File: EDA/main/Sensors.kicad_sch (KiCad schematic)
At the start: 13 parts, among them U2 ICM-42688-PC, U3 MMC5983MA, U4 TMP121AIDBVR, U5 TMP121AIDBVR, U6 BMP581

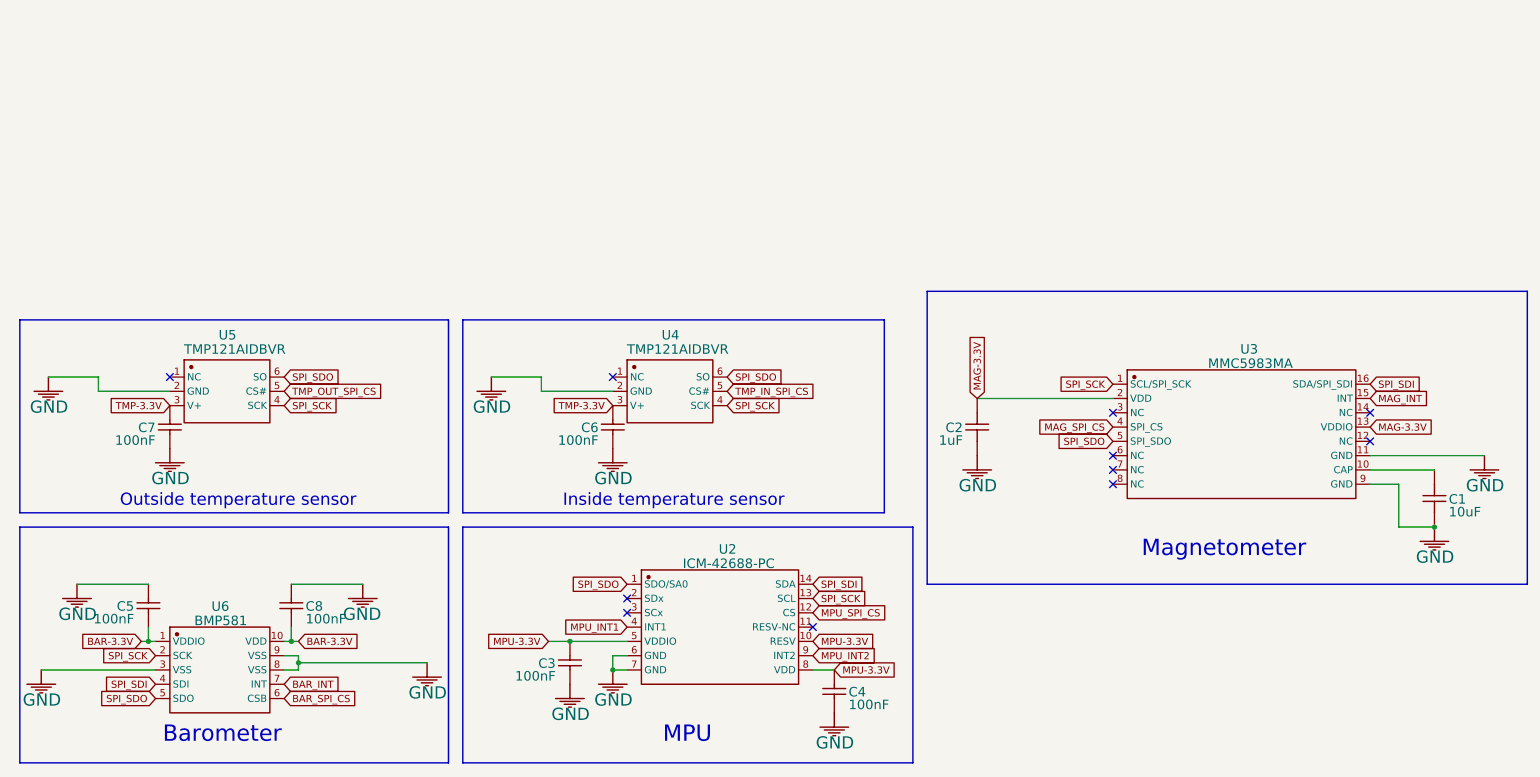
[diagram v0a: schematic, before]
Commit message: Project restructure, and added a bottom assembly PCB.
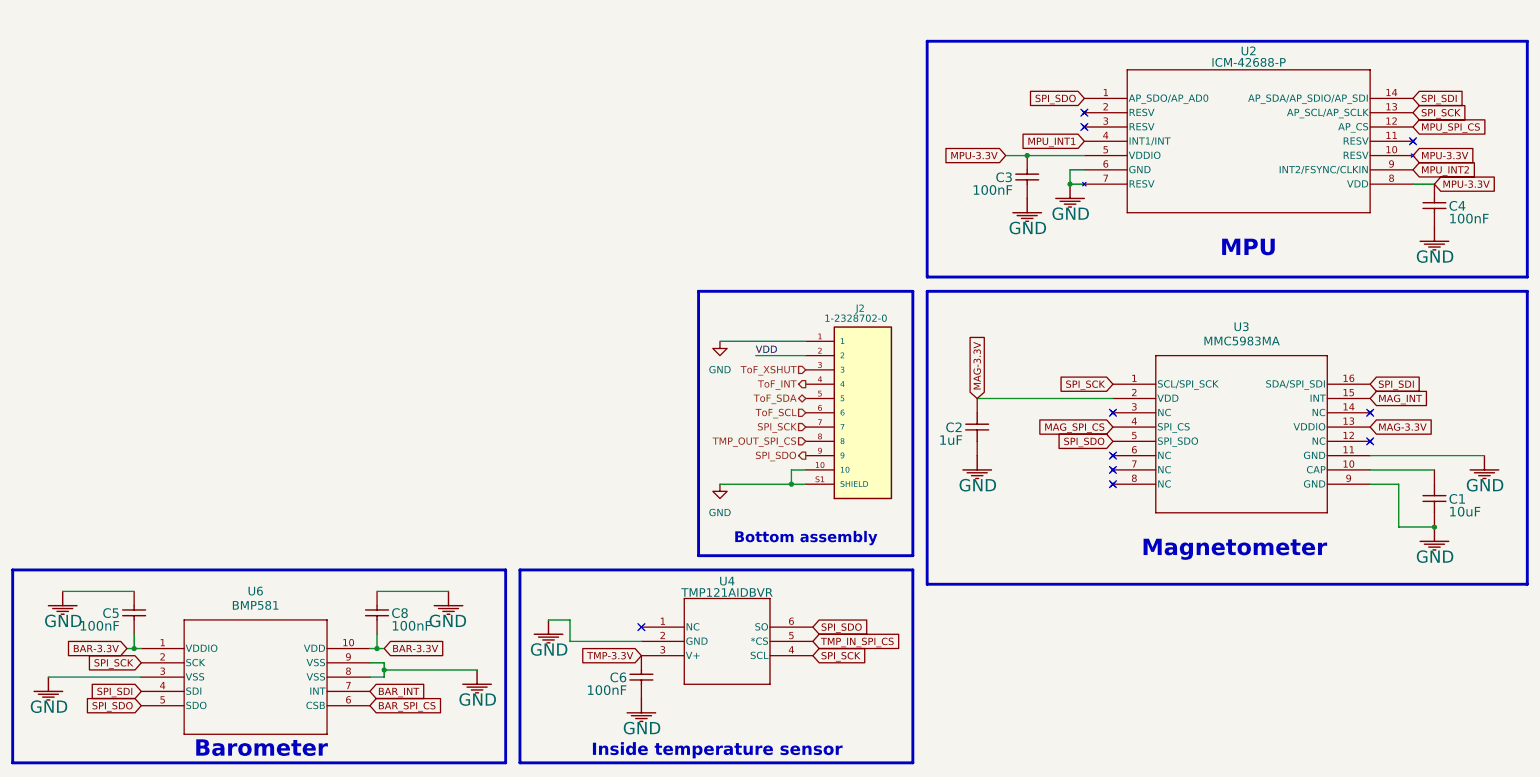
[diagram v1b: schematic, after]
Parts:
- removed C7: 100nF, symbol CL10B104JB8NNNC_4
- removed U2: ICM-42688-PC, symbol ICM-42688-PC
- removed U3: MMC5983MA, symbol MMC5983MA
- removed U4: TMP121AIDBVR, symbol TMP121AIDBVR
- removed U5: TMP121AIDBVR, symbol TMP121AIDBVR_1
- removed U6: BMP581, symbol BMP581
- added J2: 1-2328702-0, CANSAT-lib:TE_1-2328702-0, symbol CANSAT-lib:1-2328702-0
- added U2: ICM-42688-P, CANSAT-lib:LGA14_2P5X3X0P91_TDK, symbol CANSAT-lib:ICM-42688-P
- added U3: MMC5983MA, CANSAT-lib:MMC5983MA_MEM, symbol CANSAT-lib:MMC5983MA
- added U4: TMP121AIDBVR, CANSAT-lib:DBV6, symbol CANSAT-lib:TMP121AIDBVR
- added U6: BMP581, CANSAT-lib:QFN10_BMP581_BOS, symbol CANSAT-lib:BMP581
- C1, C2: footprint (none) -> Capacitor_SMD:C_0603_1608Metric
- C3, C4, C5, C6, C8: footprint (none) -> Capacitor_SMD:C_0402_1005Metric
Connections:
- net BAR-3.3V: now also U6.1 (VDDIO), U6.10 (VDD)
- net BAR_INT: now also U6.7 (INT)
- net BAR_SPI_CS: now also U6.6 (CSB)
- net GND: now also J2.1, J2.10, J2.S1 (SHIELD), J2.S2 (SHIELD), U2.6 (GND), U2.7 (RESV), U3.11 (GND), U3.9 (GND), U4.2 (GND), U6.3 (VSS), U6.8 (VSS), U6.9 (VSS)
- net MAG-3.3V: now also U3.13 (VDDIO), U3.2 (VDD)
- net MAG_INT: now also U3.15 (INT)
- net MAG_SPI_CS: now also U3.4 (SPI_CS)
- net MPU-3.3V: now also U2.10 (RESV), U2.5 (VDDIO), U2.8 (VDD)
- net MPU_INT1: now also U2.4 (INT1/INT)
- net MPU_INT2: now also U2.9 (INT2/FSYNC/CLKIN)
- net MPU_SPI_CS: now also U2.12 (AP_CS)
- net SPI_SCK: now also J2.7, U2.13 (AP_SCL/AP_SCLK), U3.1 (SCL/SPI_SCK), U4.4 (SCL), U6.2 (SCK)
- net SPI_SDI: now also U2.14 (AP_SDA/AP_SDIO/AP_SDI), U3.16 (SDA/SPI_SDI), U6.4 (SDI)
- net SPI_SDO: now also J2.9, U2.1 (AP_SDO/AP_AD0), U3.5 (SPI_SDO), U4.6 (SO), U6.5 (SDO)
- net TMP-3.3V: now also U4.3 (V+)
- net TMP_IN_SPI_CS: now also U4.5 (*CS)
- net TMP_OUT_SPI_CS: now also J2.8
- net at C1.2: now also U3.10 (CAP)
- new net ToF_INT: J2.4
- new net ToF_SCL: J2.6
- new net ToF_SDA: J2.5
- new net ToF_XSHUT: J2.3
- new net VDD: J2.2
- no-connect marks 11 -> 10
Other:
- note added: "Bottom assembly"
- note removed: "Outside temperature sensor"
- moved on the sheet: C3, C4, C5, C6, C8

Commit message: Assigned CS and INT from sensors, and added SWD to PWR-MCU and CORE-MCU
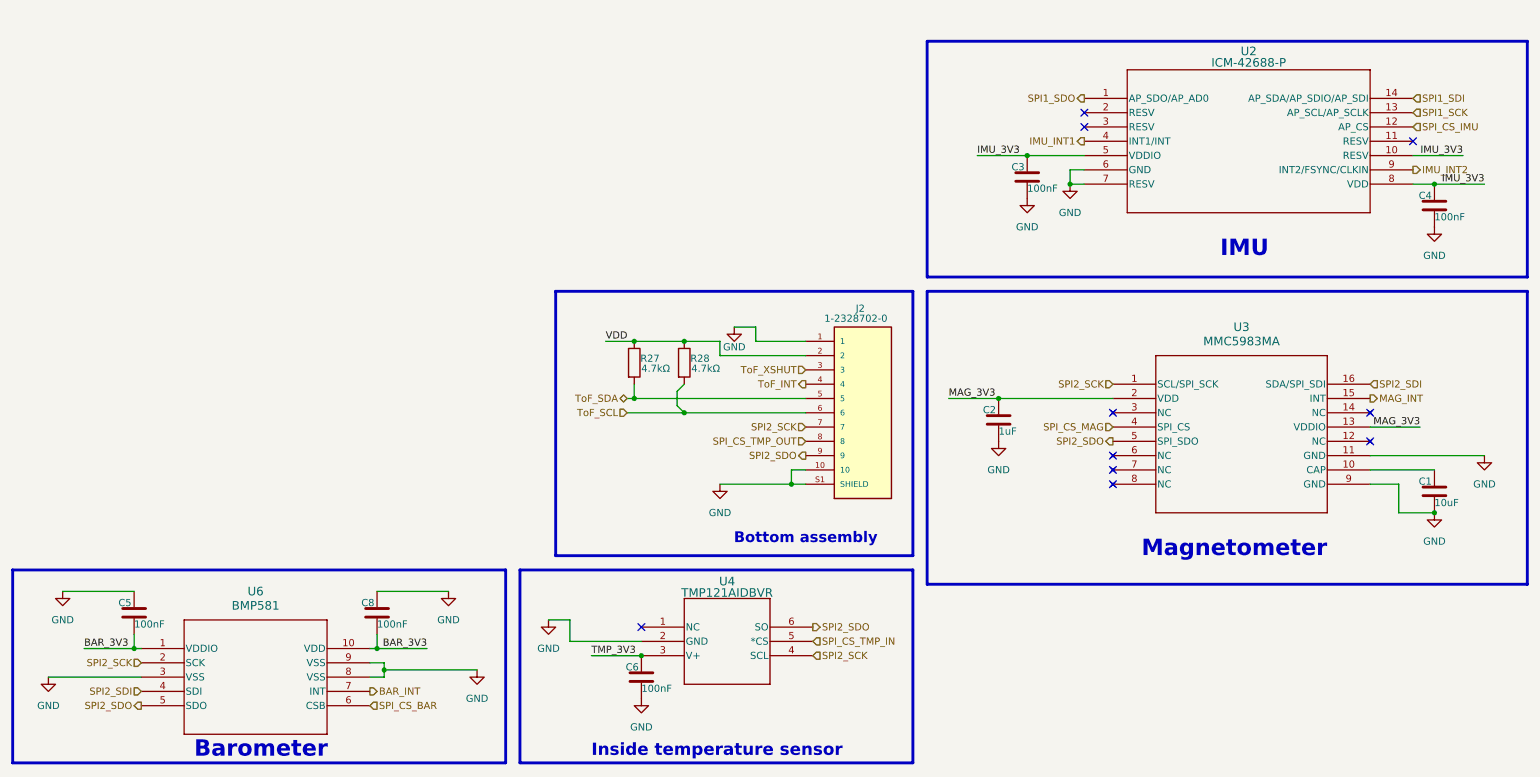
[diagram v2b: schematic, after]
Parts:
- removed C1: 10uF, Capacitor_SMD:C_0603_1608Metric, symbol C0805C106J8RACAUTO7210
- removed C2: 1uF, Capacitor_SMD:C_0603_1608Metric, symbol CC0805JKX7R9BB105
- removed C3: 100nF, Capacitor_SMD:C_0402_1005Metric, symbol CL10B104JB8NNNC
- removed C4: 100nF, Capacitor_SMD:C_0402_1005Metric, symbol CL10B104JB8NNNC_1
- removed C5: 100nF, Capacitor_SMD:C_0402_1005Metric, symbol CL10B104JB8NNNC_2
- removed C6: 100nF, Capacitor_SMD:C_0402_1005Metric, symbol CL10B104JB8NNNC_3
- removed C8: 100nF, Capacitor_SMD:C_0402_1005Metric, symbol CL10B104JB8NNNC_5
- added C1: 10uF, Capacitor_SMD:C_0603_1608Metric, symbol Device:C
- added C2: 1uF, Capacitor_SMD:C_0603_1608Metric, symbol Device:C
- added C3, C4, C5, C6, C8: 100nF, Capacitor_SMD:C_0402_1005Metric, symbol Device:C
- added R27, R28: 4.7kΩ, Resistor_SMD:R_0402_1005Metric, symbol Device:R
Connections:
- net GND: now also C1.2, C2.2, C3.2, C4.2, C5.1, C6.2, C8.1
- net ToF_SCL: now also R28.2
- net ToF_SDA: now also R27.2
- net VDD: now also R27.1, R28.1
- net at U3.10 (CAP): now also C1.1
- net BAR-3.3V renamed BAR_3V3
- net BAR_3V3: now also C5.2, C8.2
- net BAR_SPI_CS renamed SPI_CS_BAR
- net MAG-3.3V renamed MAG_3V3
- net MAG_3V3: now also C2.1
- net MAG_SPI_CS renamed SPI_CS_MAG
- net MPU-3.3V renamed IMU_3V3
- net IMU_3V3: now also C3.1, C4.1
- net MPU_INT1 renamed IMU_INT1
- net MPU_INT2 renamed IMU_INT2
- net MPU_SPI_CS renamed SPI_CS_IMU
- net SPI_SCK renamed SPI2_SCK
- net SPI2_SCK: no longer U2.13 (AP_SCL/AP_SCLK)
- net SPI_SDI renamed SPI2_SDI
- net SPI2_SDI: no longer U2.14 (AP_SDA/AP_SDIO/AP_SDI)
- net SPI_SDO renamed SPI2_SDO
- net SPI2_SDO: no longer U2.1 (AP_SDO/AP_AD0)
- net TMP-3.3V renamed TMP_3V3
- net TMP_3V3: now also C6.1
- net TMP_IN_SPI_CS renamed SPI_CS_TMP_IN
- net TMP_OUT_SPI_CS renamed SPI_CS_TMP_OUT
- new net SPI1_SCK: U2.13 (AP_SCL/AP_SCLK)
- new net SPI1_SDI: U2.14 (AP_SDA/AP_SDIO/AP_SDI)
- new net SPI1_SDO: U2.1 (AP_SDO/AP_AD0)
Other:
- note added: "IMU"
- note removed: "MPU"

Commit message: Uploaded work
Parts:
- added C106, C108: 1uF, Capacitor_SMD:C_0603_1608Metric, symbol Device:C
- added C107: 10uF, Capacitor_SMD:C_0603_1608Metric, symbol Device:C
- added U5: TPS22919DCKR, CANSAT-lib:SOT65P210X110-6N, symbol CANSAT-lib:TPS22919DCKR
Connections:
- net IMU_3V3 is gone; now on net 3V3: C3.1, C4.1, U2.10 (RESV), U2.5 (VDDIO), U2.8 (VDD)
- net MAG_3V3 is gone; now on net 3V3: C2.1, U3.13 (VDDIO), U3.2 (VDD)
- net TMP_3V3 is gone; now on net 3V3: C6.1, U4.3 (V+)
- net VDD is gone; now on net 3V3: J2.2, R27.1, R28.1
- net GND: now also C106.2, C107.2, C108.2, U5.2 (GND)
- net BAR_3V3 renamed 3V3
- net 3V3: now also C106.1, C107.1, C108.1, U5.1 (IN), U5.5 (QOD), U5.6 (VOUT)
- new net SENS_EN: U5.3 (ON)
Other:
- note added: "PWR SW"

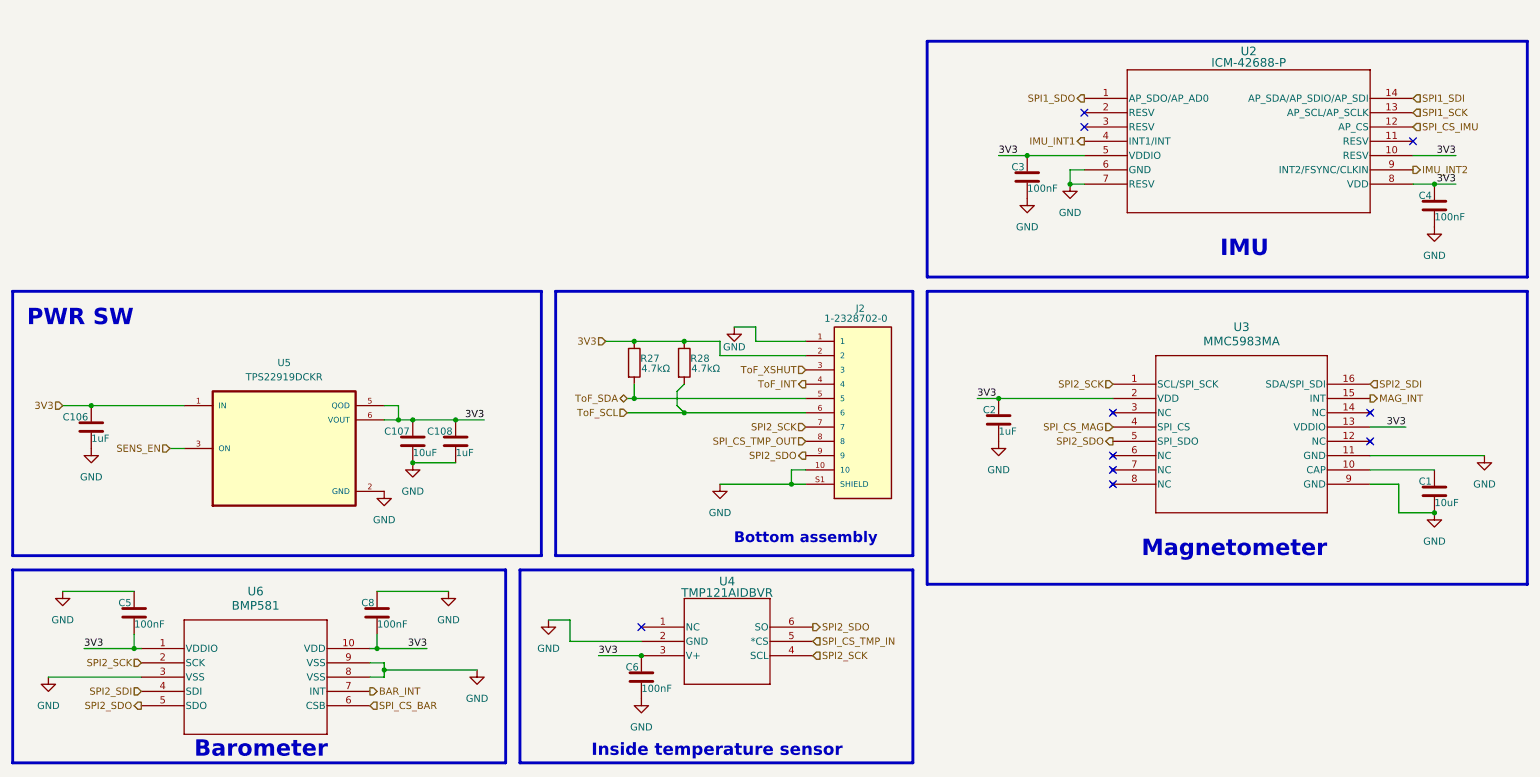
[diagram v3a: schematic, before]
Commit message: Finished gas sensor PCB, and added connector for it on main PCB
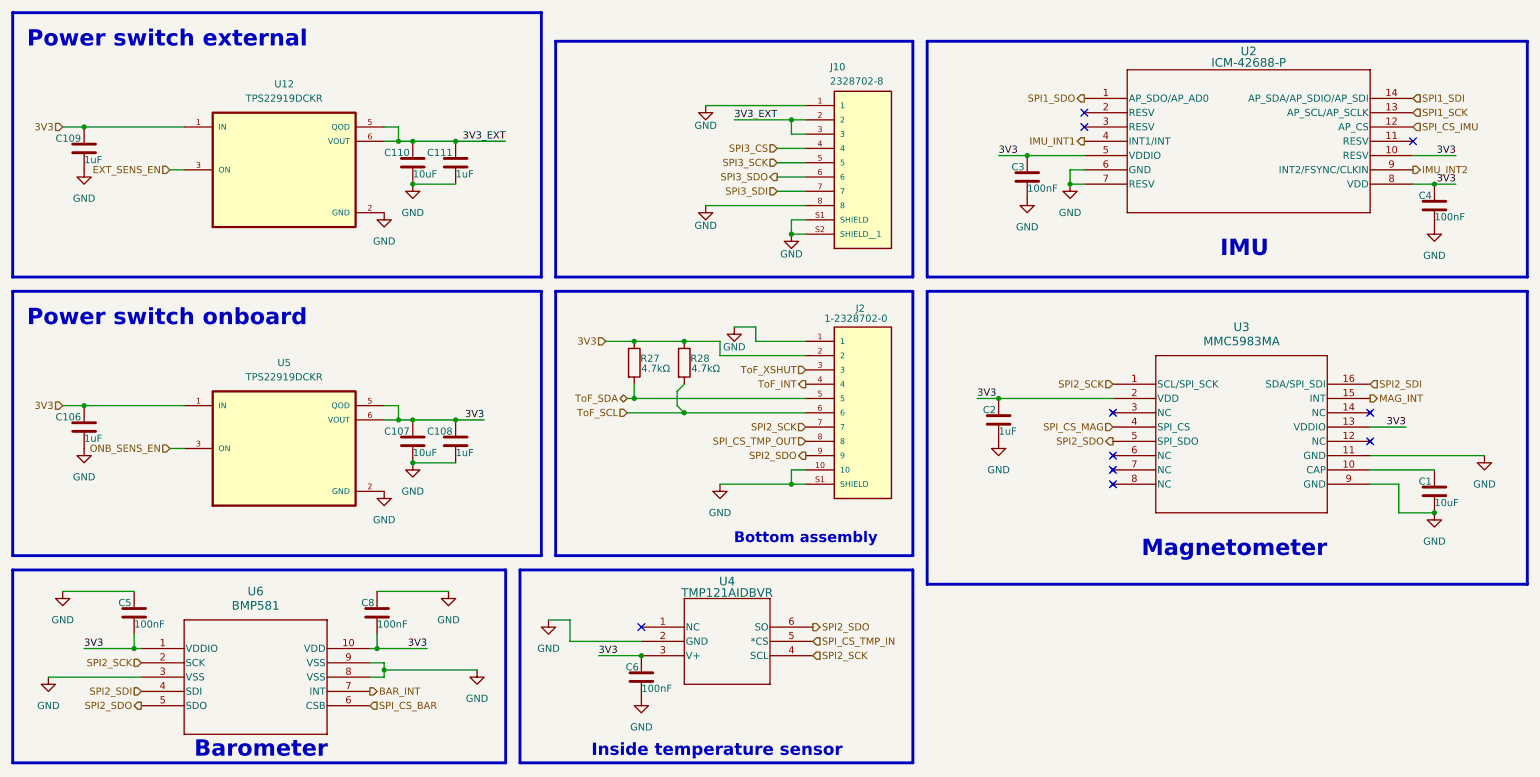
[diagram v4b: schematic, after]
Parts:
- added C109, C111: 1uF, Capacitor_SMD:C_0603_1608Metric, symbol Device:C
- added C110: 10uF, Capacitor_SMD:C_0603_1608Metric, symbol Device:C
- added J10: 2328702-8, CANSAT-lib:TE_2328702-8, symbol CANSAT-lib:2328702-8
- added U12: TPS22919DCKR, CANSAT-lib:SOT65P210X110-6N, symbol CANSAT-lib:TPS22919DCKR
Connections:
- net 3V3: now also C109.1, U12.1 (IN)
- net GND: now also C109.2, C110.2, C111.2, J10.1, J10.8, J10.S1 (SHIELD), J10.S2 (SHIELD__1), U12.2 (GND)
- net SENS_EN renamed ONB_SENS_EN
- new net 3V3_EXT: C110.1, C111.1, J10.2, J10.3, U12.5 (QOD), U12.6 (VOUT)
- new net EXT_SENS_EN: U12.3 (ON)
- new net SPI3_CS: J10.4
- new net SPI3_SCK: J10.5
- new net SPI3_SDI: J10.7
- new net SPI3_SDO: J10.6
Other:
- note added: "Power switch external"
- note added: "Power switch onboard"
- note removed: "PWR SW"
- moved on the sheet: C106

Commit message: Uploaded work
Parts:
- removed R27, R28: 4.7kΩ, Resistor_SMD:R_0402_1005Metric, symbol Device:R
